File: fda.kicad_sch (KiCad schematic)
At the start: 42 parts, among them U706 OPA2197D, U73 OPA2388DGK, U74 THS4521IDGK

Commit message: Scan deleted.
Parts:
- C729, C730: LCSC C1546? -> C32949
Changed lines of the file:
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@@
 			)
 		)
-		(property "Datasheet" "50V"
+		(property "Datasheet" "X7R, 50V"
 			(at 179.07 69.85 0)
 			(effects
@@
 			)
 		)
-		(property "LCSC" "C1546?"
+		(property "LCSC" "C32949"
 			(at 74.93 149.86 0)
 			(effects
@@
 			)
 		)
-		(property "LCSC" "C1546?"
+		(property "LCSC" "C32949"
 			(at 74.93 58.42 0)
 			(effects
@@
 			)
 		)
-		(property "Datasheet" "50V"
+		(property "Datasheet" "X7R, 50V"
 			(at 179.07 77.47 0)
 			(effects

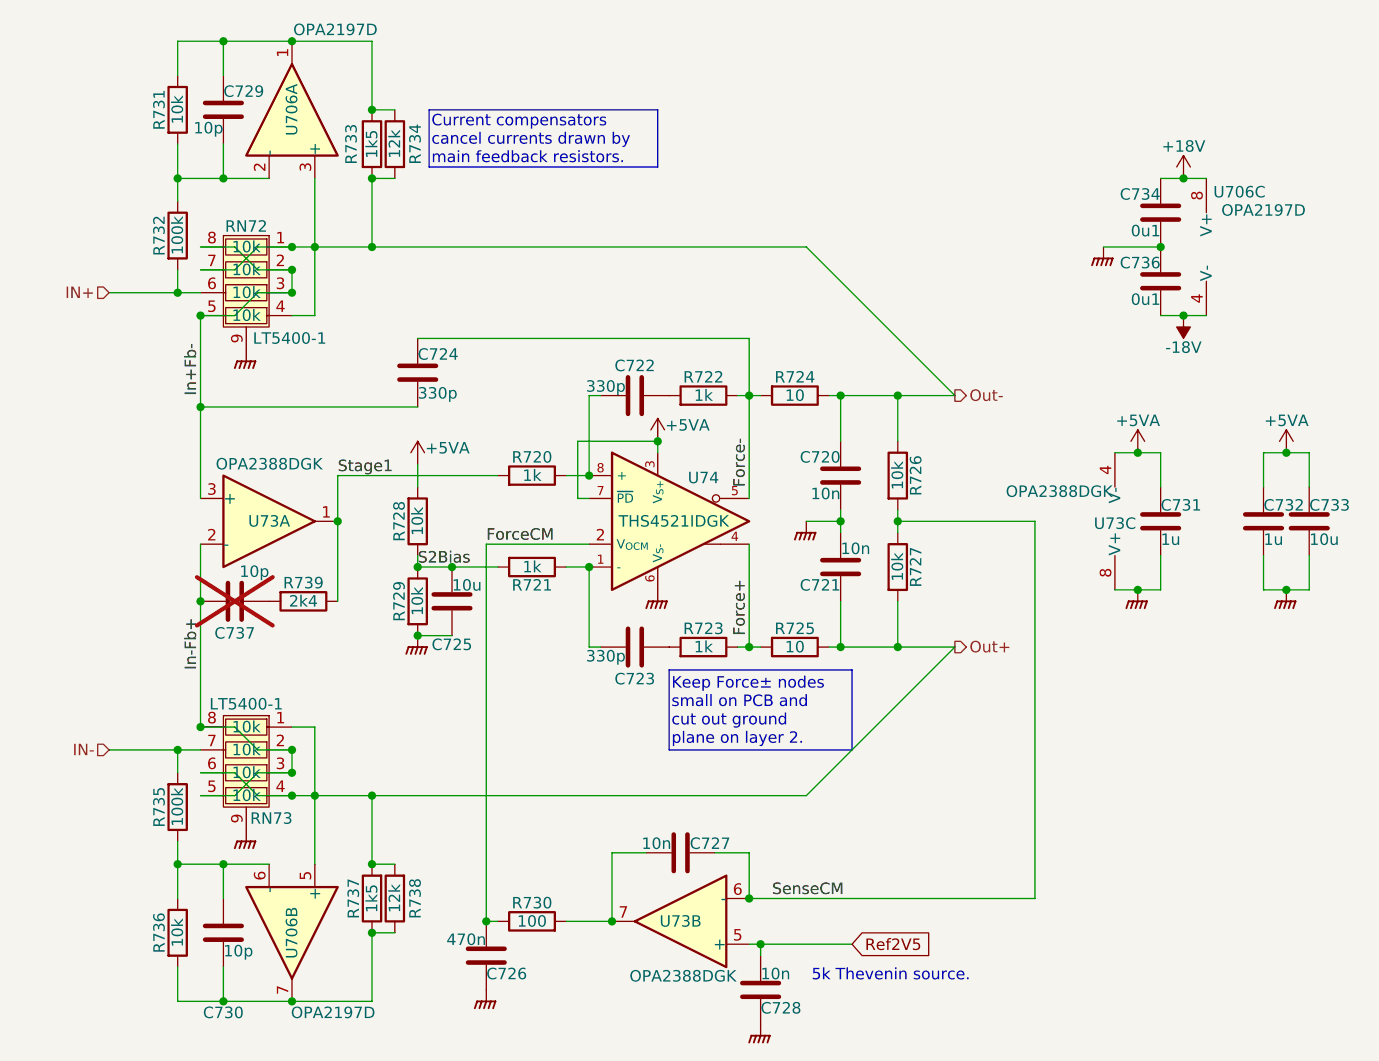
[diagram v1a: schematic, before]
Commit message: Put ref filtering into the schematic.
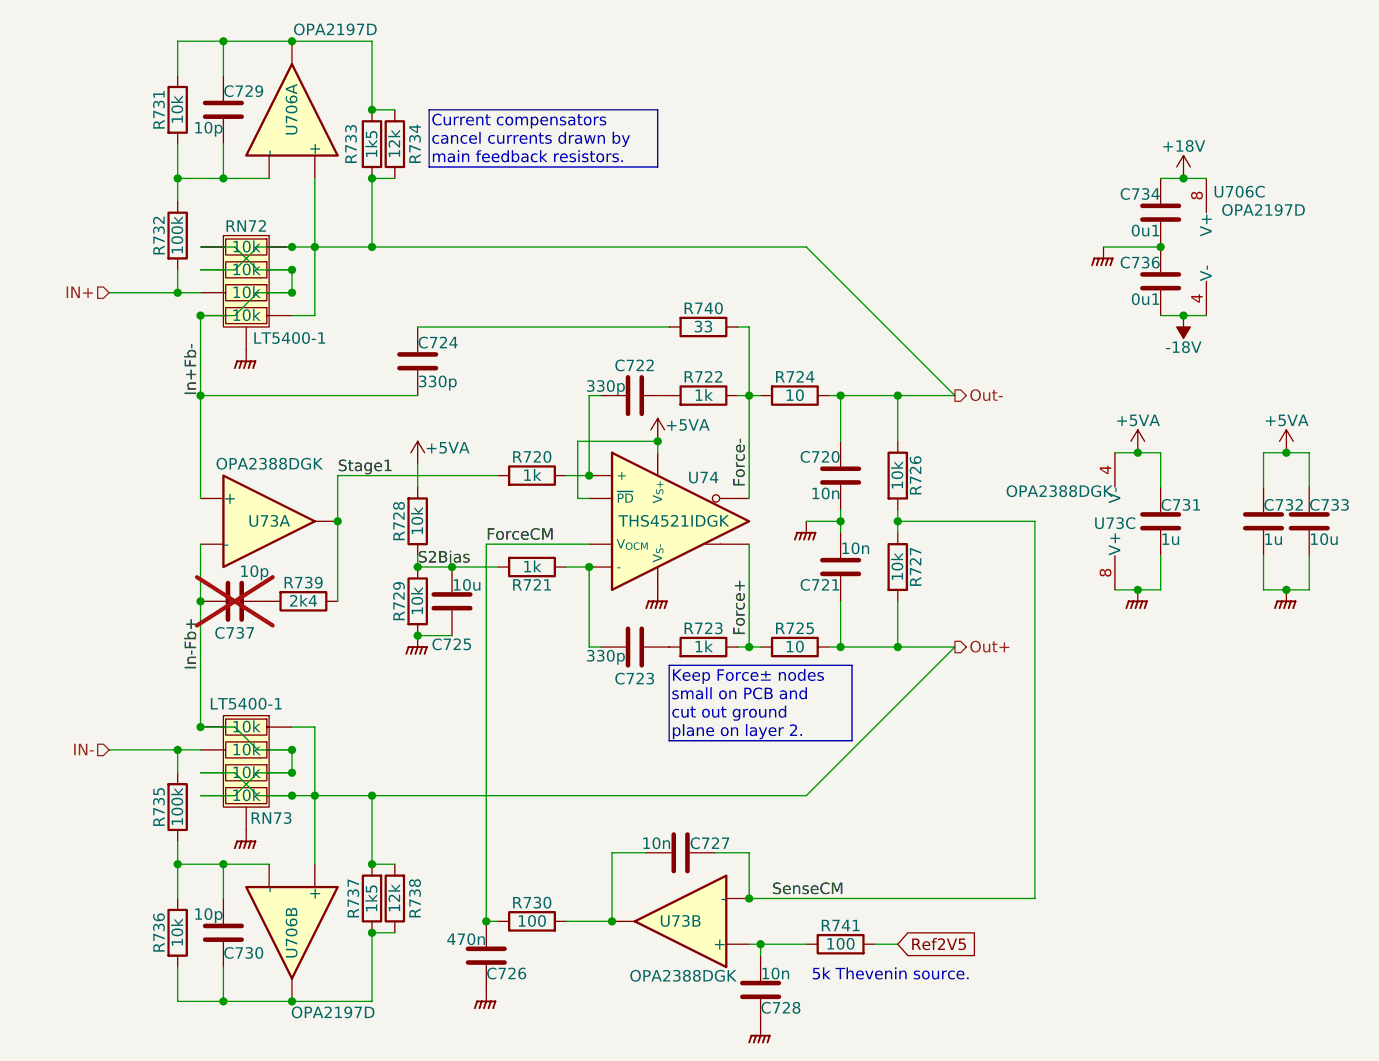
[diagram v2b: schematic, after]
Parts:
- added R740: 33, Resistor_SMD:R_0402_1005Metric, symbol Device:R
- added R741: 100, Resistor_SMD:R_0402_1005Metric, symbol Device:R
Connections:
- net Force-: now also R740.1; no longer C724.2
- net Ref2V5: now also R741.2; no longer C728.1, U73.5 (+)
- new net: C728.1, R741.1, U73.5 (+)
- new net: C724.2, R740.2
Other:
- moved on the sheet: C724
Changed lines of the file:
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@@
 	(text_box "Keep Force± nodes small on PCB and cut out ground plane on layer 2."
 		(exclude_from_sim no)
-		(at 124.46 120.65 0)
-		(size 20.3199 8.89)
+		(at 124.46 120.142 0)
+		(size 20.3199 8.382)
 		(margins 0.254 0.254 0.254 0.254)
 		(stroke
@@
 	)
 	(junction
-		(at 72.39 91.44)
-		(diameter 0)
-		(color 0 0 0 0)
-	)
-	(junction
 		(at 87.63 104.14)
 		(diameter 0)
@@
 		(color 0 0 0 0)
 	)
+	(junction
+		(at 72.39 90.17)
+		(diameter 0)
+		(color 0 0 0 0)
+	)
 	(wire
 		(pts
@@
 	(wire
 		(pts
-			(xy 72.39 91.44) (xy 72.39 101.6)
+			(xy 72.39 90.17) (xy 72.39 101.6)
 		)
 		(stroke
@@
 	(wire
 		(pts
-			(xy 134.62 151.13) (xy 144.78 151.13)
+			(xy 134.62 151.13) (xy 139.7 151.13)
 		)
 		(stroke
@@
 	(wire
 		(pts
+			(xy 147.32 151.13) (xy 149.86 151.13)
+		)
+		(stroke
+			(width 0)
+			(type default)
+		)
+	)
+	(wire
+		(pts
 			(xy 76.2 132.08) (xy 78.74 134.62)
 		)
@@
 	(wire
 		(pts
-			(xy 72.39 81.28) (xy 72.39 91.44)
+			(xy 72.39 81.28) (xy 72.39 90.17)
 		)
 		(stroke
@@
 	(wire
 		(pts
-			(xy 72.39 91.44) (xy 96.52 91.44)
+			(xy 72.39 90.17) (xy 96.52 90.17)
 		)
 		(stroke
@@
 	(wire
 		(pts
+			(xy 132.08 82.55) (xy 133.35 82.55)
+		)
+		(stroke
+			(width 0)
+			(type default)
+		)
+	)
+	(wire
+		(pts
 			(xy 76.2 81.28) (xy 78.74 78.74)
 		)
@@
 	(wire
 		(pts
-			(xy 133.35 83.82) (xy 133.35 90.17)
+			(xy 133.35 82.55) (xy 133.35 90.17)
 		)
 		(stroke
@@
 	(wire
 		(pts
-			(xy 96.52 83.82) (xy 133.35 83.82)
+			(xy 96.52 82.55) (xy 124.46 82.55)
 		)
 		(stroke
@@
 	(global_label "Ref2V5"
 		(shape input)
-		(at 144.78 151.13 0)
+		(at 149.86 151.13 0)
 		(fields_autoplaced yes)
 		(effects
@@
 		)
 		(property "Intersheetrefs" "${INTERSHEET_REFS}"
-			(at 153.1476 151.13 0)
+			(at 158.2276 151.13 0)
 			(effects
 				(font
@@
 	)
 	(symbol
+		(lib_id "Device:R")
+		(at 128.27 82.55 270)
+		(unit 1)
+		(exclude_from_sim no)
+		(in_bom yes)
+		(on_board yes)
+		(dnp no)
+		(property "Reference" "R740"
+			(at 128.27 80.518 90)
+			(effects
+				(font
+					(size 1.27 1.27)
+				)
+			)
+		)
+		(property "Value" "33"
+			(at 128.27 82.55 90)
+			(effects
+				(font
+					(size 1.27 1.27)
+				)
+			)
+		)
+		(property "Footprint" "Resistor_SMD:R_0402_1005Metric"
+			(at 128.27 80.772 90)
+			(effects
+				(font
+					(size 1.27 1.27)
+				)
+				(hide yes)
+			)
+		)
+		(property "Datasheet" "~"
+			(at 128.27 82.55 0)
+			(effects
+				(font
+					(size 1.27 1.27)
+				)
+				(hide yes)
+			)
+		)
+		(property "Description" "Resistor"
+			(at 128.27 82.55 0)
+			(effects
+				(font
+					(size 1.27 1.27)
+				)
+				(hide yes)
+			)
+		)
+		(property "LCSC" ""
+			(at 128.27 82.55 90)
+			(effects
+				(font
+					(size 1.27 1.27)
+				)
+				(hide yes)
+			)
+		)
+		(property "Stock" ""
+			(at 128.27 82.55 90)
+			(effects
+				(font
+					(size 1.27 1.27)
+				)
+				(hide yes)
+			)
+		)
+		(pin "2"
+		)
+		(pin "1"
+		)
+		(instances
+			(project "lincal"
+				(path "/b054cef4-39e3-49d8-aff0-7ba5a206c187/91ba7742-b0d4-4498-bde0-79d5f38f349f"
+					(reference "R740")
+					(unit 1)
+				)
+			)
+		)
+	)
+	(symbol
 		(lib_id "Amplifier_Difference:THS4521IDGK")
 		(at 125.73 104.14 0)
@@
 	)
 	(symbol
+		(lib_name "OPA2388DGK_1")
 		(lib_id "Parts:OPA2388DGK")
 		(at 125.73 148.59 180)
@@
 		(dnp no)
 		(property "Reference" "C730"
-			(at 74.93 158.75 0)
+			(at 74.93 152.146 0)
 			(effects
 				(font
 					(size 1.27 1.27)
 				)
+				(justify left)
 			)
 		)
 		(property "Value" "10p"
-			(at 74.93 151.892 0)
+			(at 74.93 147.828 0)
 			(effects
 				(font
 					(size 1.27 1.27)
 				)
-				(justify left)
+				(justify right)
 			)
 		)
@@
 	)
 	(symbol
+		(lib_name "OPA2197D_2")
 		(lib_id "Parts:OPA2197D")
 		(at 82.55 58.42 270)
@@
 	(symbol
 		(lib_id "Device:C")
-		(at 96.52 87.63 180)
+		(at 96.52 86.36 180)
 		(unit 1)
 		(exclude_from_sim no)
@@
 		(dnp no)
 		(property "Reference" "C724"
-			(at 96.52 85.598 0)
+			(at 96.52 84.328 0)
 			(effects
 				(font
@@
 		)
 		(property "Value" "330p"
-			(at 96.52 89.916 0)
+			(at 96.52 88.646 0)
 			(effects
 				(font
@@
 		)
 		(property "Footprint" "Capacitor_SMD:C_0603_1608Metric"
-			(at 95.5548 83.82 0)
+			(at 95.5548 82.55 0)
 			(effects
 				(font
@@
 		)
 		(property "Datasheet" "C0G, 50V"
-			(at 96.52 87.63 0)
+			(at 96.52 86.36 0)
 			(effects
 				(font
@@
 		)
 		(property "Description" "Unpolarized capacitor"
-			(at 96.52 87.63 0)
+			(at 96.52 86.36 0)
 			(effects
 				(font
@@
 		)
 		(property "LCSC" "C1664"
-			(at 96.52 87.63 90)
+			(at 96.52 86.36 90)
 			(effects
 				(font
@@
 		)
 		(property "Stock" ""
-			(at 96.52 87.63 0)
+			(at 96.52 86.36 0)
 			(effects
 				(font
@@
 	)
 	(symbol
+		(lib_name "LT5400_1")
 		(lib_id "Parts:LT5400")
 		(at 77.47 78.74 0)
@@
 	)
 	(symbol
+		(lib_name "OPA2197D_1")
 		(lib_id "Parts:OPA2197D")
 		(at 82.55 149.86 270)
@@
 	)
 	(symbol
+		(lib_id "Device:R")
+		(at 143.51 151.13 90)
+		(unit 1)
+		(exclude_from_sim no)
+		(in_bom yes)
+		(on_board yes)
+		(dnp no)
+		(property "Reference" "R741"
+			(at 143.51 149.098 90)
+			(effects
+				(font
+					(size 1.27 1.27)
+				)
+			)
+		)
+		(property "Value" "100"
+			(at 143.51 151.13 90)
+			(effects
+				(font
+					(size 1.27 1.27)
+				)
+			)
+		)
+		(property "Footprint" "Resistor_SMD:R_0402_1005Metric"
+			(at 143.51 152.908 90)
+			(effects
+				(font
+					(size 1.27 1.27)
+				)
+				(hide yes)
+			)
+		)
+		(property "Datasheet" "~"
+			(at 143.51 151.13 0)
+			(effects
+				(font
+					(size 1.27 1.27)
+				)
+				(hide yes)
+			)
+		)
+		(property "Description" "Resistor"
+			(at 143.51 151.13 0)
+			(effects
+				(font
+					(size 1.27 1.27)
+				)
+				(hide yes)
+			)
+		)
+		(property "LCSC" "C25076"
+			(at 143.51 151.13 90)
+			(effects
+				(font
+					(size 1.27 1.27)
+				)
+				(hide yes)
+			)
+		)
+		(property "Stock" ""
+			(at 143.51 151.13 90)
+			(effects
+				(font
+					(size 1.27 1.27)
+				)
+				(hide yes)
+			)
+		)
+		(pin "2"
+		)
+		(pin "1"
+		)
+		(instances
+			(project "lincal"
+				(path "/b054cef4-39e3-49d8-aff0-7ba5a206c187/91ba7742-b0d4-4498-bde0-79d5f38f349f"
+					(reference "R741")
+					(unit 1)
+				)
+			)
+		)
+	)
+	(symbol
 		(lib_id "Device:C")
 		(at 190.5 104.14 0)
@@
 	)
 	(symbol
+		(lib_name "OPA2388DGK_2")
 		(lib_id "Parts:OPA2388DGK")
 		(at 80.01 104.14 0)

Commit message: Adjust voltage rails.
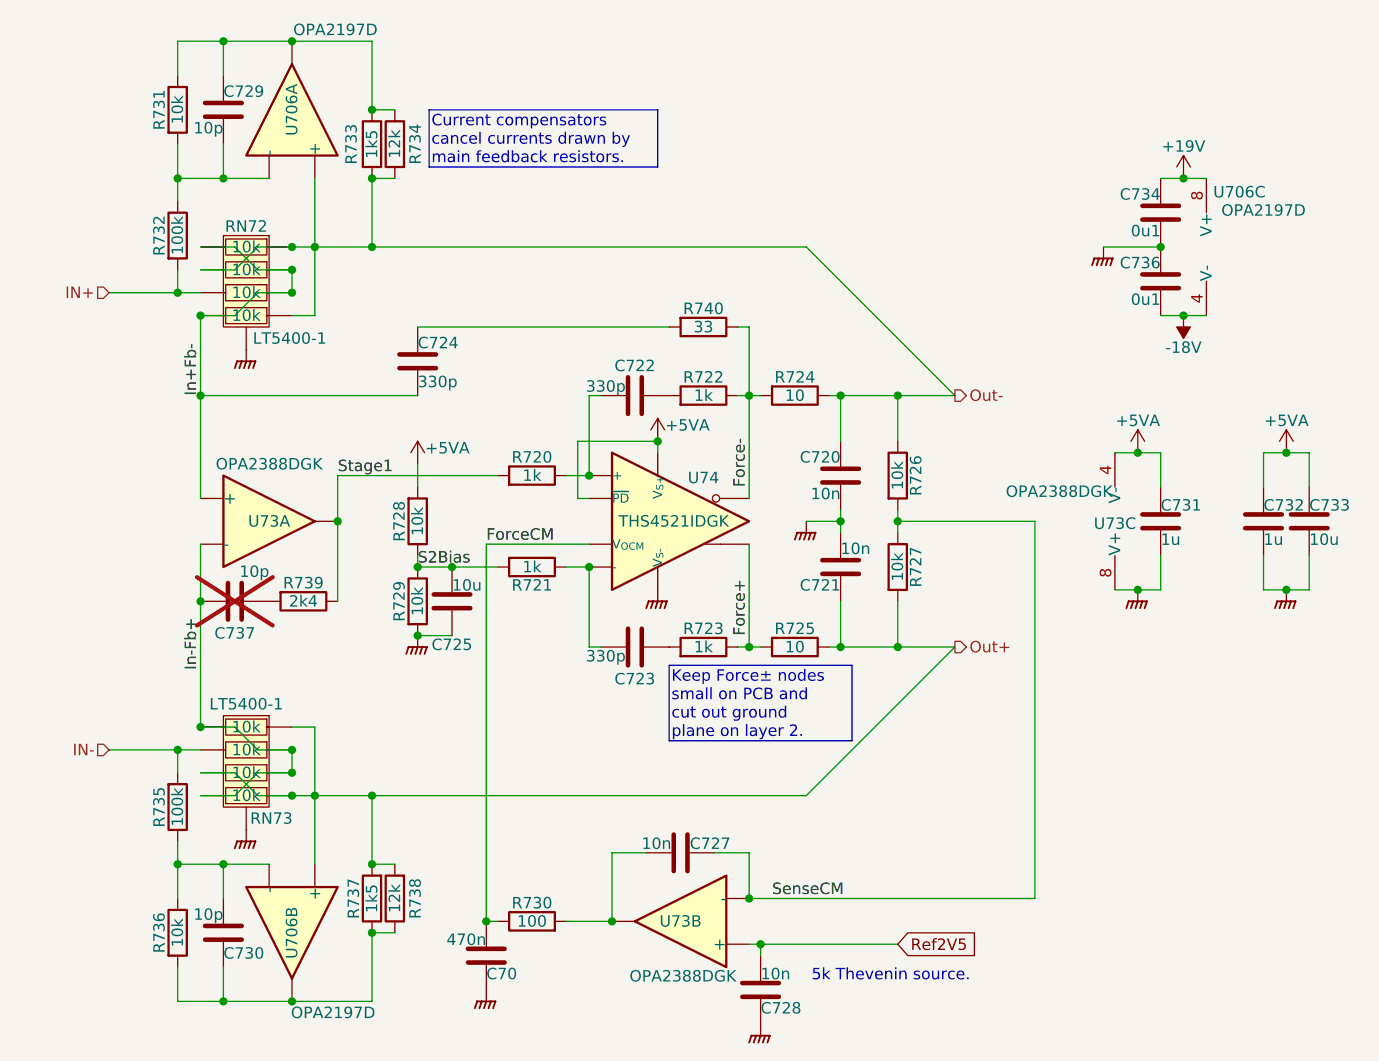
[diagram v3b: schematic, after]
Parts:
- removed R741: 100, Resistor_SMD:R_0402_1005Metric, symbol Device:R
- U74: footprint Parts:OPA4521 -> Parts:THS4521; symbol Amplifier_Difference:THS4521IDGK -> Parts:THS4521IDGK
- renumbered C726 to C70
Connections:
- net Ref2V5: now also C728.1, U73.5 (+)
- net +18V renamed +19V
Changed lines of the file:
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@@
 	(wire
 		(pts
-			(xy 134.62 151.13) (xy 139.7 151.13)
+			(xy 134.62 151.13) (xy 149.86 151.13)
 		)
 		(stroke
@@
 	(wire
 		(pts
-			(xy 147.32 151.13) (xy 149.86 151.13)
-		)
-		(stroke
-			(width 0)
-			(type default)
-		)
-	)
-	(wire
-		(pts
 			(xy 76.2 132.08) (xy 78.74 134.62)
 		)
@@
 	)
 	(symbol
-		(lib_id "Amplifier_Difference:THS4521IDGK")
+		(lib_id "Parts:THS4521IDGK")
 		(at 125.73 104.14 0)
 		(unit 1)
@@
 			)
 		)
-		(property "Footprint" "Parts:OPA4521"
+		(property "Footprint" "Parts:THS4521"
 			(at 125.73 123.19 0)
 			(effects
@@
 		(on_board yes)
 		(dnp no)
-		(property "Reference" "C726"
+		(property "Reference" "C70"
 			(at 104.14 154.432 0)
 			(effects
@@
 			(project "lincal"
 				(path "/b054cef4-39e3-49d8-aff0-7ba5a206c187/91ba7742-b0d4-4498-bde0-79d5f38f349f"
-					(reference "C726")
+					(reference "C70")
 					(unit 1)
 				)
@@
 	)
 	(symbol
-		(lib_id "Parts:+18V")
+		(lib_id "Parts:+19V")
 		(at 181.61 66.04 0)
 		(unit 1)
@@
 		(on_board yes)
 		(dnp no)
-		(property "Reference" "#PWR0148"
+		(property "Reference" "#PWR148"
 			(at 181.61 69.85 0)
 			(effects
@@
 			)
 		)
-		(property "Value" "+18V"
+		(property "Value" "+19V"
 			(at 181.61 62.484 0)
 			(do_not_autoplace yes)
@@
 			)
 		)
-		(property "Description" "Power symbol creates a global label with name {dblquote}+18V{dblquote}"
+		(property "Description" "Power symbol creates a global label with name \"+19\""
 			(at 181.61 66.04 0)
 			(effects
@@
 			(project "lincal"
 				(path "/b054cef4-39e3-49d8-aff0-7ba5a206c187/91ba7742-b0d4-4498-bde0-79d5f38f349f"
-					(reference "#PWR0148")
+					(reference "#PWR148")
 					(unit 1)
 				)
@@
 				)
 			)
-		)
-	)
-	(symbol
-		(lib_id "Device:R")
-		(at 143.51 151.13 90)
-		(unit 1)
-		(exclude_from_sim no)
-		(in_bom yes)
-		(on_board yes)
-		(dnp no)
-		(property "Reference" "R741"
-			(at 143.51 149.098 90)
-			(effects
-				(font
-					(size 1.27 1.27)
-				)
-			)
-		)
-		(property "Value" "100"
-			(at 143.51 151.13 90)
-			(effects
-				(font
-					(size 1.27 1.27)
-				)
-			)
-		)
-		(property "Footprint" "Resistor_SMD:R_0402_1005Metric"
-			(at 143.51 152.908 90)
-			(effects
-				(font
-					(size 1.27 1.27)
-				)
-				(hide yes)
-			)
-		)
-		(property "Datasheet" "~"
-			(at 143.51 151.13 0)
-			(effects
-				(font
-					(size 1.27 1.27)
-				)
-				(hide yes)
-			)
-		)
-		(property "Description" "Resistor"
-			(at 143.51 151.13 0)
-			(effects
-				(font
-					(size 1.27 1.27)
-				)
-				(hide yes)
-			)
-		)
-		(property "LCSC" "C25076"
-			(at 143.51 151.13 90)
-			(effects
-				(font
-					(size 1.27 1.27)
-				)
-				(hide yes)
-			)
-		)
-		(property "Stock" ""
-			(at 143.51 151.13 90)
-			(effects
-				(font
-					(size 1.27 1.27)
-				)
-				(hide yes)
-			)
-		)
-		(pin "2"
-		)
-		(pin "1"
-		)
-		(instances
-			(project "lincal"
-				(path "/b054cef4-39e3-49d8-aff0-7ba5a206c187/91ba7742-b0d4-4498-bde0-79d5f38f349f"
-					(reference "R741")
-					(unit 1)
-				)
-			)
